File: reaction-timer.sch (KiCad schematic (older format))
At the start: 33 parts, among them IC1 4026, IC2 4026, IC3 4026, IC5 NE555P, IC6 NE555P, IC7 NE555P

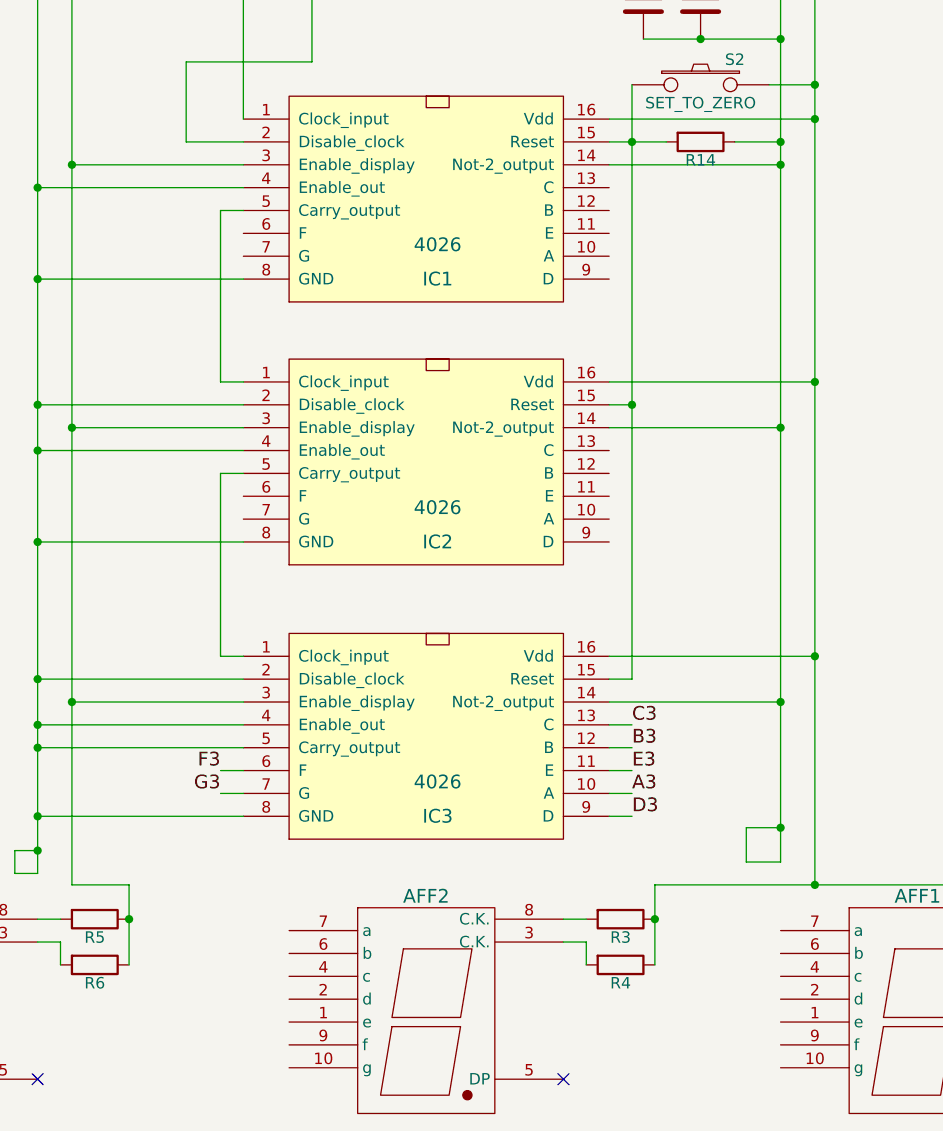
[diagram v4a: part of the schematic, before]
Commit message: Connect all 7-seg displays to driver chips
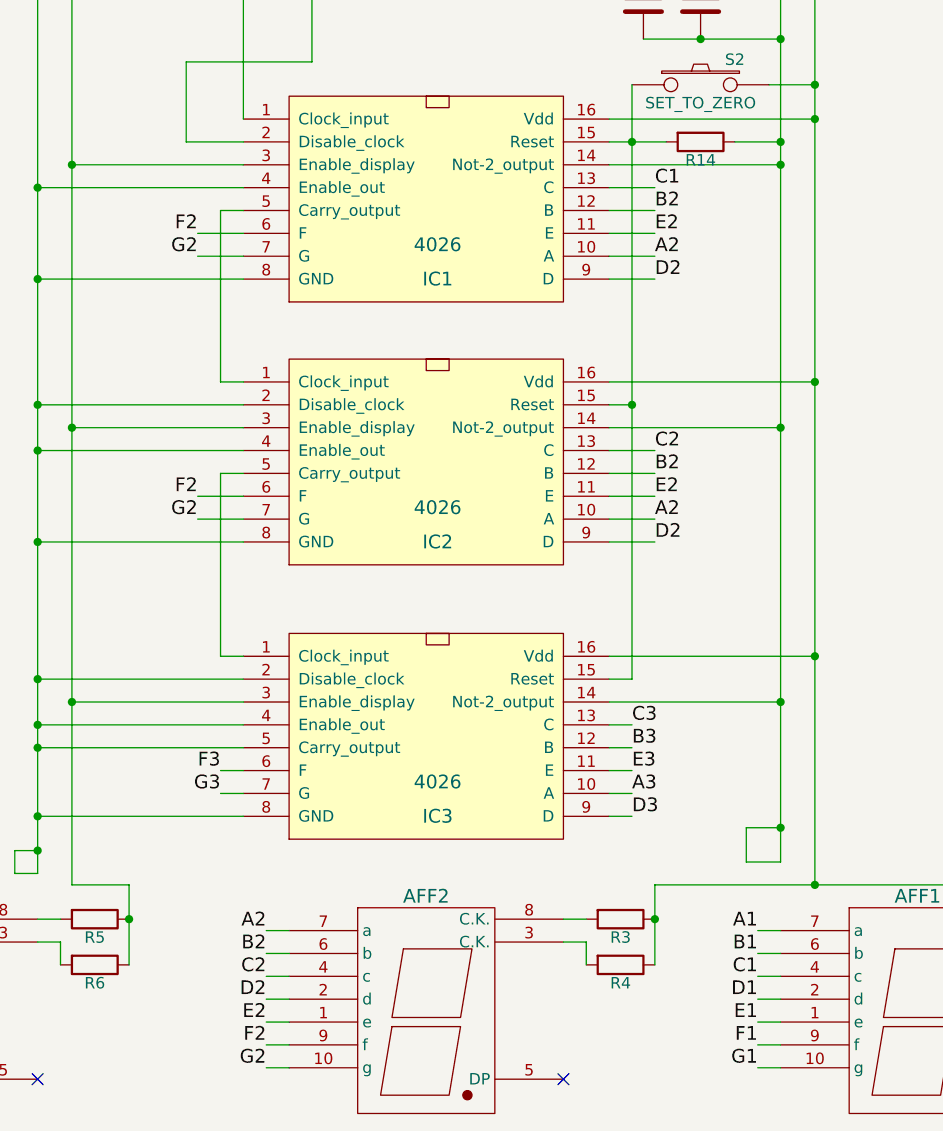
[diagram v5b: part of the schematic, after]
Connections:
- net A2: now reaches IC1.10 (A)
- net A2: now also AFF2.7 (a), IC2.10 (A)
- net E2: now reaches IC1.11 (E)
- net E2: now also AFF2.1 (e), IC2.11 (E)
- net B2: now reaches IC1.12 (B)
- net B2: now also AFF2.6 (b), IC2.12 (B)
- net C1: now reaches IC1.13 (C)
- net C1: now also AFF1.4 (c)
- net F2: now reaches IC1.6 (F)
- net F2: now also AFF2.9 (f), IC2.6 (F)
- net G2: now reaches IC1.7 (G)
- net G2: now also AFF2.10 (g), IC2.7 (G)
- net D2: now reaches IC1.9 (D)
- net D2: now also AFF2.2 (d), IC2.9 (D)
- net C2: now reaches IC2.13 (C)
- net C2: now also AFF2.4 (c)
- net E1: now reaches AFF1.1 (e)
- net G1: now reaches AFF1.10 (g)
- net D1: now reaches AFF1.2 (d)
- net B1: now reaches AFF1.6 (b)
- net A1: now reaches AFF1.7 (a)
- net F1: now reaches AFF1.9 (f)
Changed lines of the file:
@@
 Wire Wire Line
 	5000 8100 5100 8100
+Text Label 3200 7100 2    60   ~ 0
+F2
+Text Label 3200 7200 2    60   ~ 0
+G2
+Text Label 5200 6900 0    60   ~ 0
+C2
+Text Label 5200 7000 0    60   ~ 0
+B2
+Text Label 5200 7100 0    60   ~ 0
+E2
+Text Label 5200 7200 0    60   ~ 0
+A2
+Text Label 5200 7300 0    60   ~ 0
+D2
+Text Label 5200 5750 0    60   ~ 0
+C1
+Text Label 5200 5850 0    60   ~ 0
+B2
+Text Label 5200 5950 0    60   ~ 0
+E2
+Text Label 5200 6050 0    60   ~ 0
+A2
+Text Label 5200 6150 0    60   ~ 0
+D2
+Text Label 3200 5950 2    60   ~ 0
+F2
+Text Label 3200 6050 2    60   ~ 0
+G2
+Wire Wire Line
+	3200 5950 3400 5950
+Wire Wire Line
+	3400 6050 3200 6050
+Wire Wire Line
+	5000 5750 5200 5750
+Wire Wire Line
+	5200 5850 5000 5850
+Wire Wire Line
+	5000 5950 5200 5950
+Wire Wire Line
+	5200 6050 5000 6050
+Wire Wire Line
+	5000 6150 5200 6150
+Wire Wire Line
+	5200 6900 5000 6900
+Wire Wire Line
+	5000 7000 5200 7000
+Wire Wire Line
+	5200 7100 5000 7100
+Wire Wire Line
+	5000 7200 5200 7200
+Wire Wire Line
+	5200 7300 5000 7300
+Text Label 3500 9000 2    60   ~ 0
+A2
+Text Label 3500 9100 2    60   ~ 0
+B2
+Text Label 3500 9200 2    60   ~ 0
+C2
+Text Label 3500 9300 2    60   ~ 0
+D2
+Text Label 3500 9400 2    60   ~ 0
+E2
+Text Label 3500 9500 2    60   ~ 0
+F2
+Text Label 3500 9600 2    60   ~ 0
+G2
+Wire Wire Line
+	3500 9600 3600 9600
+Wire Wire Line
+	3600 9500 3500 9500
+Wire Wire Line
+	3500 9400 3600 9400
+Wire Wire Line
+	3600 9300 3500 9300
+Wire Wire Line
+	3500 9200 3600 9200
+Wire Wire Line
+	3600 9100 3500 9100
+Wire Wire Line
+	3500 9000 3600 9000
+Text Label 5650 9000 2    60   ~ 0
+A1
+Text Label 5650 9100 2    60   ~ 0
+B1
+Text Label 5650 9200 2    60   ~ 0
+C1
+Text Label 5650 9300 2    60   ~ 0
+D1
+Text Label 5650 9400 2    60   ~ 0
+E1
+Text Label 5650 9500 2    60   ~ 0
+F1
+Text Label 5650 9600 2    60   ~ 0
+G1
+Wire Wire Line
+	5650 9600 5750 9600
+Wire Wire Line
+	5750 9500 5650 9500
+Wire Wire Line
+	5650 9400 5750 9400
+Wire Wire Line
+	5750 9300 5650 9300
+Wire Wire Line
+	5650 9200 5750 9200
+Wire Wire Line
+	5750 9100 5650 9100
+Wire Wire Line
+	5650 9000 5750 9000
+Wire Wire Line
+	3200 7100 3400 7100
+Wire Wire Line
+	3400 7200 3200 7200
 $EndSCHEMATC

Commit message: Fix bugs in connection labeling
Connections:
- net A1: now also IC1.10 (A)
- net A2: no longer IC1.10 (A)
- net B1: now also IC1.12 (B)
- net B2: no longer IC1.12 (B)
- net D1: now also IC1.9 (D)
- net D2: no longer IC1.9 (D)
- net E1: now also IC1.11 (E)
- net E2: no longer IC1.11 (E)
- net F1: now also IC1.6 (F)
- net F2: no longer IC1.6 (F)
- net G1: now also IC1.7 (G)
- net G2: no longer IC1.7 (G)
- net GNDREF renamed GND
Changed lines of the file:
@@
-$EndComp
-$Comp
-L GNDREF #PWR02
-U 1 1 557465F3
-P 5750 900
-F 0 "#PWR02" H 5750 650 50  0001 C CNN
-F 1 "GNDREF" H 5750 750 50  0000 C CNN
-F 2 "" H 5750 900 60  0000 C CNN
-F 3 "" H 5750 900 60  0000 C CNN
-	1    5750 900
-	-1   0    0    1
 $EndComp
 $Comp
@@
 Connection ~ 5750 1050
 Wire Wire Line
-	2650 950  5900 950
+	2350 950  5900 950
 Wire Wire Line
 	5300 1300 5200 1300
@@
 	5250 4800 5400 4800
 Wire Wire Line
-	5000 5450 5900 5450
-Connection ~ 5900 5450
-Wire Wire Line
 	5700 5300 5900 5300
 Connection ~ 5900 5300
@@
 	3400 8500 2500 8500
 Connection ~ 2500 8500
-Wire Wire Line
-	5000 5650 5750 5650
-Connection ~ 5750 5650
 Wire Wire Line
 	5000 6600 5900 6600
@@
 C1
 Text Label 5200 5850 0    60   ~ 0
-B2
+B1
 Text Label 5200 5950 0    60   ~ 0
-E2
+E1
 Text Label 5200 6050 0    60   ~ 0
-A2
+A1
 Text Label 5200 6150 0    60   ~ 0
-D2
+D1
 Text Label 3200 5950 2    60   ~ 0
-F2
+F1
 Text Label 3200 6050 2    60   ~ 0
-G2
+G1
 Wire Wire Line
 	3200 5950 3400 5950
@@
 G1
 Wire Wire Line
+	3200 7100 3400 7100
+Wire Wire Line
+	3400 7200 3200 7200
+Wire Wire Line
+	5000 5450 5900 5450
+Connection ~ 5900 5450
+Wire Wire Line
+	5000 5650 5750 5650
+Connection ~ 5750 5650
+$Comp
+L GND #PWR02
+U 1 1 5577F775
+P 5750 900
+F 0 "#PWR02" H 5750 650 50  0001 C CNN
+F 1 "GND" H 5750 750 50  0000 C CNN
+F 2 "" H 5750 900 60  0000 C CNN
+F 3 "" H 5750 900 60  0000 C CNN
+	1    5750 900
+	-1   0    0    1
+$EndComp
+$Comp
+L PWR_FLAG #FLG03
+U 1 1 5577FCD2
+P 2350 950
+F 0 "#FLG03" H 2350 1045 50  0001 C CNN
+F 1 "PWR_FLAG" H 2350 1130 50  0000 C CNN
+F 2 "" H 2350 950 60  0000 C CNN
+F 3 "" H 2350 950 60  0000 C CNN
+	1    2350 950
+	0    -1   -1   0
+$EndComp
+Wire Wire Line
 	5650 9600 5750 9600
 Wire Wire Line
 	5750 9500 5650 9500
 Wire Wire Line
-	5650 9400 5750 9400
+	5750 9400 5650 9400
 Wire Wire Line
 	5750 9300 5650 9300
 Wire Wire Line
-	5650 9200 5750 9200
+	5750 9200 5650 9200
 Wire Wire Line
 	5750 9100 5650 9100
 Wire Wire Line
-	5650 9000 5750 9000
-Wire Wire Line
-	3200 7100 3400 7100
-Wire Wire Line
-	3400 7200 3200 7200
+	5750 9000 5650 9000
 $EndSCHEMATC

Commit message: Add reverse voltage protection diode
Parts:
- added D1: D, symbol D
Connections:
- net +9V: now also D1.2 (A); no longer C1.1, IC1.16 (Vdd), IC1.3 (Enable_display), IC2.16 (Vdd), IC2.3 (Enable_display), IC3.16 (Vdd), IC3.3 (Enable_display), IC5.4 (RESET), IC5.8 (Vcc), IC6.6 (THRES), IC6.8 (Vcc), IC7.4 (RESET), IC7.8 (Vcc), R1.1, R10.2, R11.1, R12.1, R13.2, R2.1, R3.1, R4.1, R5.1, R6.1, R7.1, R9.2, S2.2
- new net: C1.1, D1.1 (K), IC1.16 (Vdd), IC1.3 (Enable_display), IC2.16 (Vdd), IC2.3 (Enable_display), IC3.16 (Vdd), IC3.3 (Enable_display), IC5.4 (RESET), IC5.8 (Vcc), IC6.6 (THRES), IC6.8 (Vcc), IC7.4 (RESET), IC7.8 (Vcc), R1.1, R10.2, R11.1, R12.1, R13.2, R2.1, R3.1, R4.1, R5.1, R6.1, R7.1, R9.2, S2.2

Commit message: Associate last footprints and add battery
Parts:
- added BT1: 9V_Battery, Pin_Headers:Pin_Header_Straight_1x02, symbol Battery
- AFF1, AFF2, AFF3: footprint (none) -> Displays_7-Segment:7SegmentLED_LTS6760_LTS6780
- C1: footprint (none) -> Capacitors_Elko_ThroughHole:Elko_vert_11x5mm_RM2.5
- C2, C3, C4, C6: footprint (none) -> Capacitors_ThroughHole:C_Disc_D7.5_P5
- C5: footprint (none) -> Capacitors_Elko_ThroughHole:Elko_vert_11x5mm_RM2
- D1: footprint (none) -> Diodes_ThroughHole:Diode_DO-41_SOD81_Horizontal_RM10
- IC1, IC2, IC3: footprint (none) -> Housings_DIP:DIP-16_W7.62mm_LongPads
- IC5, IC6, IC7: footprint (none) -> Housings_DIP:DIP-8_W7.62mm_LongPads
- LED1: footprint (none) -> LEDs:LED-5MM
- R1, R10, R11, R12, R13, R14, R2, R3, R4, R5, R6, R7, R9: footprint (none) -> Resistors_ThroughHole:Resistor_Horizontal_RM10mm
- R8: footprint (none) -> Potentiometers:Potentiometer_Bourns_3296W_3-8Zoll_Inline_ScrewUp
- S2, S3, S4: footprint (none) -> Wire_Pads:SolderWirePad_2x_1mmDrill
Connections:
- net +9V: now also BT1.1
- net GND: now also BT1.2
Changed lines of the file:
@@
 F 0 "S4" H 3550 1410 50  0000 C CNN
 F 1 "START_DELAY" H 3400 1220 50  0000 C CNN
-F 2 "" H 3400 1300 60  0000 C CNN
+F 2 "Wire_Pads:SolderWirePad_2x_1mmDrill" H 3400 1300 60  0001 C CNN
 F 3 "" H 3400 1300 60  0000 C CNN
 	1    3400 1300
@@
 F 0 "IC7" H 4500 2050 60  0000 C CNN
 F 1 "NE555P" H 4500 2250 60  0000 C CNN
-F 2 "" H 4500 1950 60  0000 C CNN
+F 2 "Housings_DIP:DIP-8_W7.62mm_LongPads" H 4500 1950 60  0001 C CNN
 F 3 "" H 4500 1950 60  0000 C CNN
 	1    4500 1950
@@
 F 0 "IC6" H 5000 3300 60  0000 C CNN
 F 1 "NE555P" H 5000 3500 60  0000 C CNN
-F 2 "" H 5000 3200 60  0000 C CNN
+F 2 "Housings_DIP:DIP-8_W7.62mm_LongPads" H 5000 3200 60  0001 C CNN
 F 3 "" H 5000 3200 60  0000 C CNN
 	1    5000 3200
@@
 F 0 "IC5" H 4550 4550 60  0000 C CNN
 F 1 "NE555P" H 4550 4750 60  0000 C CNN
-F 2 "" H 4550 4450 60  0000 C CNN
+F 2 "Housings_DIP:DIP-8_W7.62mm_LongPads" H 4550 4450 60  0001 C CNN
 F 3 "" H 4550 4450 60  0000 C CNN
 	1    4550 4450
@@
 F 0 "C1" V 5550 1400 50  0000 L CNN
 F 1 "CP" H 5475 1200 50  0001 L CNN
-F 2 "" H 5488 1150 30  0000 C CNN
+F 2 "Capacitors_Elko_ThroughHole:Elko_vert_11x5mm_RM2.5" H 5488 1150 30  0001 C CNN
 F 3 "" H 5450 1300 60  0000 C CNN
 	1    5450 1300
@@
 F 0 "R13" V 3230 1750 50  0000 C CNN
 F 1 "R" V 3150 1750 50  0001 C CNN
-F 2 "" V 3080 1750 30  0000 C CNN
+F 2 "Resistors_ThroughHole:Resistor_Horizontal_RM10mm" V 3080 1750 30  0001 C CNN
 F 3 "" H 3150 1750 30  0000 C CNN
 	1    3150 1750
@@
 F 0 "R11" V 5530 1750 50  0000 C CNN
 F 1 "R" V 5450 1750 50  0001 C CNN
-F 2 "" V 5380 1750 30  0000 C CNN
+F 2 "Resistors_ThroughHole:Resistor_Horizontal_RM10mm" V 5380 1750 30  0001 C CNN
 F 3 "" H 5450 1750 30  0000 C CNN
 	1    5450 1750
@@
 F 0 "C5" H 5475 2150 50  0000 L CNN
 F 1 "CP" H 5475 1950 50  0001 L CNN
-F 2 "" H 5488 1900 30  0000 C CNN
+F 2 "Capacitors_Elko_ThroughHole:Elko_vert_11x5mm_RM2" H 5488 1900 30  0001 C CNN
 F 3 "" H 5450 2050 60  0000 C CNN
 	1    5450 2050
@@
 F 0 "C6" H 5175 2300 50  0000 L CNN
 F 1 "C" H 5175 2100 50  0001 L CNN
-F 2 "" H 5188 2050 30  0000 C CNN
+F 2 "Capacitors_ThroughHole:C_Disc_D7.5_P5" H 5188 2050 30  0001 C CNN
 F 3 "" H 5150 2200 60  0000 C CNN
 	1    5150 2200
@@
 F 0 "C4" H 4225 2550 50  0000 L CNN
 F 1 "C" H 4225 2350 50  0001 L CNN
-F 2 "" H 4238 2300 30  0000 C CNN
+F 2 "Capacitors_ThroughHole:C_Disc_D7.5_P5" H 4238 2300 30  0001 C CNN
 F 3 "" H 4200 2450 60  0000 C CNN
 	1    4200 2450
@@
 F 0 "R9" V 3230 3000 50  0000 C CNN
 F 1 "R" V 3150 3000 50  0001 C CNN
-F 2 "" V 3080 3000 30  0000 C CNN
+F 2 "Resistors_ThroughHole:Resistor_Horizontal_RM10mm" V 3080 3000 30  0001 C CNN
 F 3 "" H 3150 3000 30  0000 C CNN
 	1    3150 3000
@@
 F 0 "S3" H 3250 3410 50  0000 C CNN
 F 1 "STOP" H 3100 3220 50  0000 C CNN
-F 2 "" H 3100 3300 60  0000 C CNN
+F 2 "Wire_Pads:SolderWirePad_2x_1mmDrill" H 3100 3300 60  0001 C CNN
 F 3 "" H 3100 3300 60  0000 C CNN
 	1    3100 3300
@@
 F 0 "R10" V 3230 3550 50  0000 C CNN
 F 1 "R" V 3150 3550 50  0001 C CNN
-F 2 "" V 3080 3550 30  0000 C CNN
+F 2 "Resistors_ThroughHole:Resistor_Horizontal_RM10mm" V 3080 3550 30  0001 C CNN
 F 3 "" H 3150 3550 30  0000 C CNN
 	1    3150 3550
@@
 F 0 "LED1" H 5000 3700 50  0000 C CNN
 F 1 "LED" H 5000 3500 50  0001 C CNN
-F 2 "" H 5000 3600 60  0000 C CNN
+F 2 "LEDs:LED-5MM" H 5000 3600 60  0001 C CNN
 F 3 "" H 5000 3600 60  0000 C CNN
 	1    5000 3600
@@
 F 0 "R12" V 5580 3600 50  0000 C CNN
 F 1 "R" V 5500 3600 50  0001 C CNN
-F 2 "" V 5430 3600 30  0000 C CNN
+F 2 "Resistors_ThroughHole:Resistor_Horizontal_RM10mm" V 5430 3600 30  0001 C CNN
 F 3 "" H 5500 3600 30  0000 C CNN
 	1    5500 3600
@@
 F 0 "R7" V 5580 4000 50  0000 C CNN
 F 1 "R" V 5500 4000 50  0001 C CNN
-F 2 "" V 5430 4000 30  0000 C CNN
+F 2 "Resistors_ThroughHole:Resistor_Horizontal_RM10mm" V 5430 4000 30  0001 C CNN
 F 3 "" H 5500 4000 30  0000 C CNN
 	1    5500 4000
@@
 F 0 "C3" H 5175 5050 50  0000 L CNN
 F 1 "C" H 5175 4850 50  0001 L CNN
-F 2 "" H 5188 4800 30  0000 C CNN
+F 2 "Capacitors_ThroughHole:C_Disc_D7.5_P5" H 5188 4800 30  0001 C CNN
 F 3 "" H 5150 4950 60  0000 C CNN
 	1    5150 4950
@@
 F 0 "R8" H 5500 4300 50  0000 C CNN
 F 1 "POT" H 5500 4400 50  0001 C CNN
-F 2 "" H 5500 4400 60  0000 C CNN
+F 2 "Potentiometers:Potentiometer_Bourns_3296W_3-8Zoll_Inline_ScrewUp" H 5500 4400 60  0001 C CNN
 F 3 "" H 5500 4400 60  0000 C CNN
 	1    5500 4400
@@
 F 0 "C2" H 5425 5050 50  0000 L CNN
 F 1 "C" H 5425 4850 50  0001 L CNN
-F 2 "" H 5438 4800 30  0000 C CNN
+F 2 "Capacitors_ThroughHole:C_Disc_D7.5_P5" H 5438 4800 30  0001 C CNN
 F 3 "" H 5400 4950 60  0000 C CNN
 	1    5400 4950
@@
 F 0 "IC1" H 4250 5950 60  0000 C CNN
 F 1 "4026" H 4250 6100 60  0000 C CNN
-F 2 "" H 4250 6050 60  0000 C CNN
+F 2 "Housings_DIP:DIP-16_W7.62mm_LongPads" H 4250 6050 60  0001 C CNN
 F 3 "" H 4250 6050 60  0000 C CNN
 	1    4250 6050
@@
 F 0 "S2" H 5550 5410 50  0000 C CNN
 F 1 "SET_TO_ZERO" H 5400 5220 50  0000 C CNN
-F 2 "" H 5400 5300 60  0000 C CNN
+F 2 "Wire_Pads:SolderWirePad_2x_1mmDrill" H 5400 5300 60  0001 C CNN
 F 3 "" H 5400 5300 60  0000 C CNN
 	1    5400 5300
@@
 F 0 "R14" V 5480 5550 50  0000 C CNN
 F 1 "R" V 5400 5550 50  0001 C CNN
-F 2 "" V 5330 5550 30  0000 C CNN
+F 2 "Resistors_ThroughHole:Resistor_Horizontal_RM10mm" V 5330 5550 30  0001 C CNN
 F 3 "" H 5400 5550 30  0000 C CNN
 	1    5400 5550
@@
 F 0 "IC2" H 4250 7100 60  0000 C CNN
 F 1 "4026" H 4250 7250 60  0000 C CNN
-F 2 "" H 4250 7200 60  0000 C CNN
+F 2 "Housings_DIP:DIP-16_W7.62mm_LongPads" H 4250 7200 60  0001 C CNN
 F 3 "" H 4250 7200 60  0000 C CNN
 	1    4250 7200
@@
 F 0 "IC3" H 4250 8300 60  0000 C CNN
 F 1 "4026" H 4250 8450 60  0000 C CNN
-F 2 "" H 4250 8400 60  0000 C CNN
+F 2 "Housings_DIP:DIP-16_W7.62mm_LongPads" H 4250 8400 60  0001 C CNN
 F 3 "" H 4250 8400 60  0000 C CNN
 	1    4250 8400
@@
 F 0 "AFF3" H 1900 9950 60  0000 C CNN
 F 1 "LTS-6980HR" H 1900 8950 60  0001 C CNN
-F 2 "" H 1900 9400 60  0000 C CNN
+F 2 "Displays_7-Segment:7SegmentLED_LTS6760_LTS6780" H 1900 9400 60  0001 C CNN
 F 3 "" H 1900 9400 60  0000 C CNN
 	1    1900 9400
@@
 F 0 "AFF2" H 4200 9950 60  0000 C CNN
 F 1 "LTS-6980HR" H 4200 8950 60  0001 C CNN
-F 2 "" H 4200 9400 60  0000 C CNN
+F 2 "Displays_7-Segment:7SegmentLED_LTS6760_LTS6780" H 4200 9400 60  0001 C CNN
 F 3 "" H 4200 9400 60  0000 C CNN
 	1    4200 9400
@@
 F 0 "AFF1" H 6350 9950 60  0000 C CNN
 F 1 "LTS-6980HR" H 6350 8950 60  0001 C CNN
-F 2 "" H 6350 9400 60  0000 C CNN
+F 2 "Displays_7-Segment:7SegmentLED_LTS6760_LTS6780" H 6350 9400 60  0001 C CNN
 F 3 "" H 6350 9400 60  0000 C CNN
 	1    6350 9400
@@
 F 0 "R5" V 2830 8950 50  0000 C CNN
 F 1 "R" V 2750 8950 50  0001 C CNN
-F 2 "" V 2680 8950 30  0000 C CNN
+F 2 "Resistors_ThroughHole:Resistor_Horizontal_RM10mm" V 2680 8950 30  0001 C CNN
 F 3 "" H 2750 8950 30  0000 C CNN
 	1    2750 8950
@@
 F 0 "R6" V 2830 9150 50  0000 C CNN
 F 1 "R" V 2750 9150 50  0001 C CNN
-F 2 "" V 2680 9150 30  0000 C CNN
+F 2 "Resistors_ThroughHole:Resistor_Horizontal_RM10mm" V 2680 9150 30  0001 C CNN
 F 3 "" H 2750 9150 30  0000 C CNN
 	1    2750 9150
@@
 F 0 "R3" V 5130 8950 50  0000 C CNN
 F 1 "R" V 5050 8950 50  0001 C CNN
-F 2 "" V 4980 8950 30  0000 C CNN
+F 2 "Resistors_ThroughHole:Resistor_Horizontal_RM10mm" V 4980 8950 30  0001 C CNN
 F 3 "" H 5050 8950 30  0000 C CNN
 	1    5050 8950
@@
 F 0 "R4" V 5130 9150 50  0000 C CNN
 F 1 "R" V 5050 9150 50  0001 C CNN
-F 2 "" V 4980 9150 30  0000 C CNN
+F 2 "Resistors_ThroughHole:Resistor_Horizontal_RM10mm" V 4980 9150 30  0001 C CNN
 F 3 "" H 5050 9150 30  0000 C CNN
 	1    5050 9150
@@
 F 0 "R1" V 7280 8950 50  0000 C CNN
 F 1 "R" V 7200 8950 50  0001 C CNN
-F 2 "" V 7130 8950 30  0000 C CNN
+F 2 "Resistors_ThroughHole:Resistor_Horizontal_RM10mm" V 7130 8950 30  0001 C CNN
 F 3 "" H 7200 8950 30  0000 C CNN
 	1    7200 8950
@@
 F 0 "R2" V 7280 9150 50  0000 C CNN
 F 1 "R" V 7200 9150 50  0001 C CNN
-F 2 "" V 7130 9150 30  0000 C CNN
+F 2 "Resistors_ThroughHole:Resistor_Horizontal_RM10mm" V 7130 9150 30  0001 C CNN
 F 3 "" H 7200 9150 30  0000 C CNN
 	1    7200 9150
@@
 F 3 "" H 2000 850 60  0000 C CNN
 	1    2000 850
-	1    0    0    -1
+	-1   0    0    1
 $EndComp
 $Comp
@@
 F 0 "D1" H 2350 950 50  0000 C CNN
 F 1 "D" H 2350 750 50  0001 C CNN
-F 2 "" H 2350 850 60  0000 C CNN
+F 2 "Diodes_ThroughHole:Diode_DO-41_SOD81_Horizontal_RM10" H 2350 850 60  0001 C CNN
 F 3 "" H 2350 850 60  0000 C CNN
 	1    2350 850
@@
 	5000 7800 5900 7800
 Connection ~ 5900 7800
+$Comp
+L Battery BT1
+U 1 1 5577447E
+P 4300 750
+F 0 "BT1" V 4400 900 50  0000 L CNN
+F 1 "9V_Battery" V 4200 850 50  0000 L CNN
+F 2 "Pin_Headers:Pin_Header_Straight_1x02" V 4300 790 60  0001 C CNN
+F 3 "" V 4300 790 60  0000 C CNN
+	1    4300 750
+	0    -1   -1   0
+$EndComp
+Wire Wire Line
+	4150 750  1800 750
+Wire Wire Line
+	1800 750  1800 850
+Connection ~ 1800 850
+Wire Wire Line
+	4450 750  4550 750
+Wire Wire Line
+	4550 750  4550 1050
+Connection ~ 4550 1050
 $EndSCHEMATC
